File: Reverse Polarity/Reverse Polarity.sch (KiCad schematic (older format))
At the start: 16 parts, among them P1 CONN_01X04, P2 CONN_01X04, P3 CONN_01X04, P4 CONN_01X04, P5 CONN_01X04, P6 CONN_01X04, P7 CONN_01X04, P8 CONN_01X04

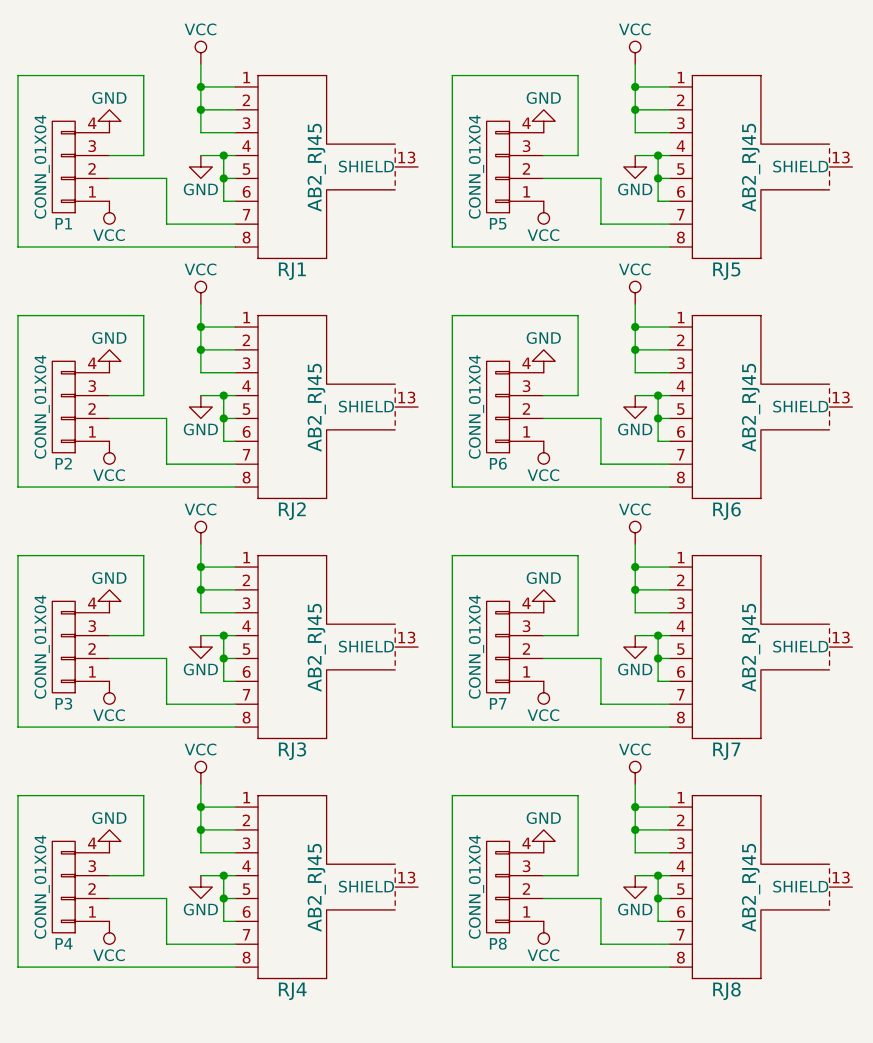
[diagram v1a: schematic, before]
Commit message: I had the ethernet plugs flopped, whoops
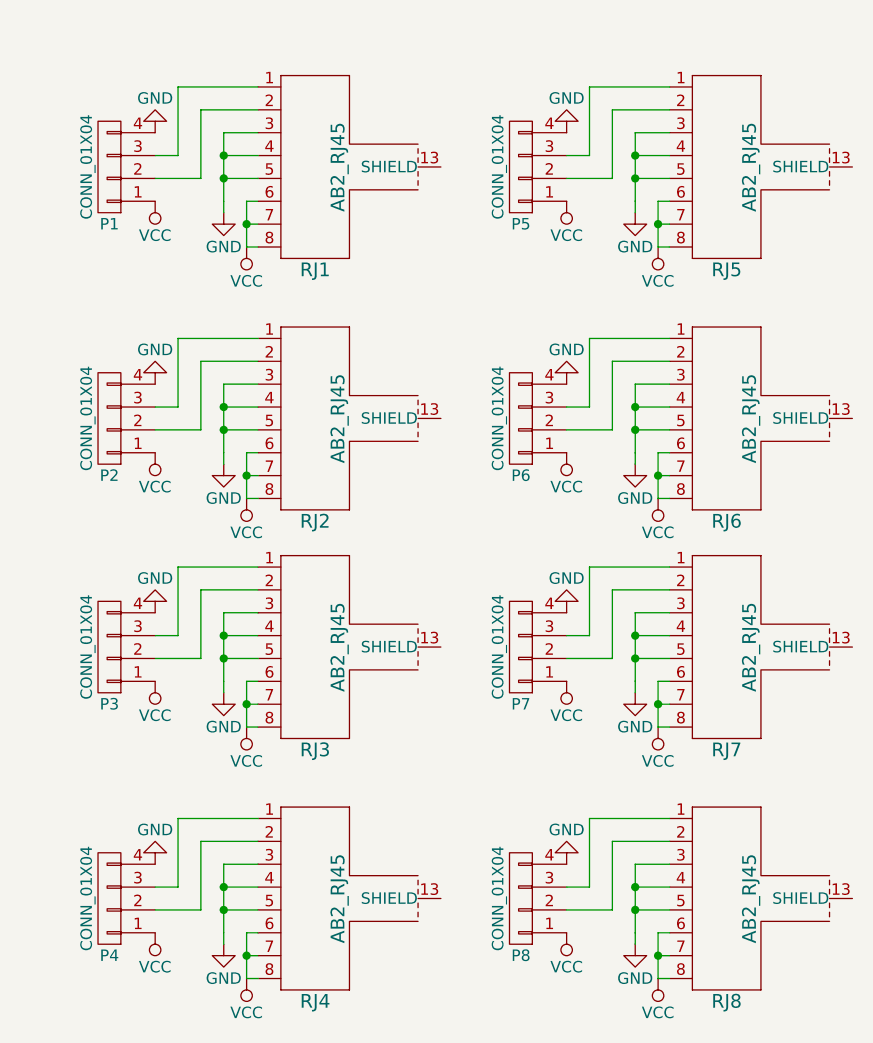
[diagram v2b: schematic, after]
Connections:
- net GND: now also RJ1.3, RJ2.3, RJ3.3, RJ4.3, RJ5.3, RJ6.3, RJ7.3, RJ8.3; no longer RJ1.6, RJ2.6, RJ3.6, RJ4.6, RJ5.6, RJ6.6, RJ7.6, RJ8.6
- net VCC: now also RJ1.6, RJ1.7, RJ1.8, RJ2.6, RJ2.7, RJ2.8, RJ3.6, RJ3.7, RJ3.8, RJ4.6, RJ4.7, RJ4.8, RJ5.6, RJ5.7, RJ5.8, RJ6.6, RJ6.7, RJ6.8, RJ7.6, RJ7.7, RJ7.8, RJ8.6, RJ8.7, RJ8.8; no longer RJ1.1, RJ1.2, RJ1.3, RJ2.1, RJ2.2, RJ2.3, RJ3.1, RJ3.2, RJ3.3, RJ4.1, RJ4.2, RJ4.3, RJ5.1, RJ5.2, RJ5.3, RJ6.1, RJ6.2, RJ6.3, RJ7.1, RJ7.2, RJ7.3, RJ8.1, RJ8.2, RJ8.3
- net at P1.2 (P2): now also RJ1.2; no longer RJ1.7
- net at P1.3 (P3): now also RJ1.1; no longer RJ1.8
- net at P2.2 (P2): now also RJ2.2; no longer RJ2.7
- net at P2.3 (P3): now also RJ2.1; no longer RJ2.8
- net at P3.2 (P2): now also RJ3.2; no longer RJ3.7
- net at P3.3 (P3): now also RJ3.1; no longer RJ3.8
- net at P4.2 (P2): now also RJ4.2; no longer RJ4.7
- net at P4.3 (P3): now also RJ4.1; no longer RJ4.8
- net at P5.2 (P2): now also RJ5.2; no longer RJ5.7
- net at P5.3 (P3): now also RJ5.1; no longer RJ5.8
- net at P6.2 (P2): now also RJ6.2; no longer RJ6.7
- net at P6.3 (P3): now also RJ6.1; no longer RJ6.8
- net at P7.2 (P2): now also RJ7.2; no longer RJ7.7
- net at P7.3 (P3): now also RJ7.1; no longer RJ7.8
- net at P8.2 (P2): now also RJ8.2; no longer RJ8.7
- net at P8.3 (P3): now also RJ8.1; no longer RJ8.8
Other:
- moved on the sheet: P1, RJ1

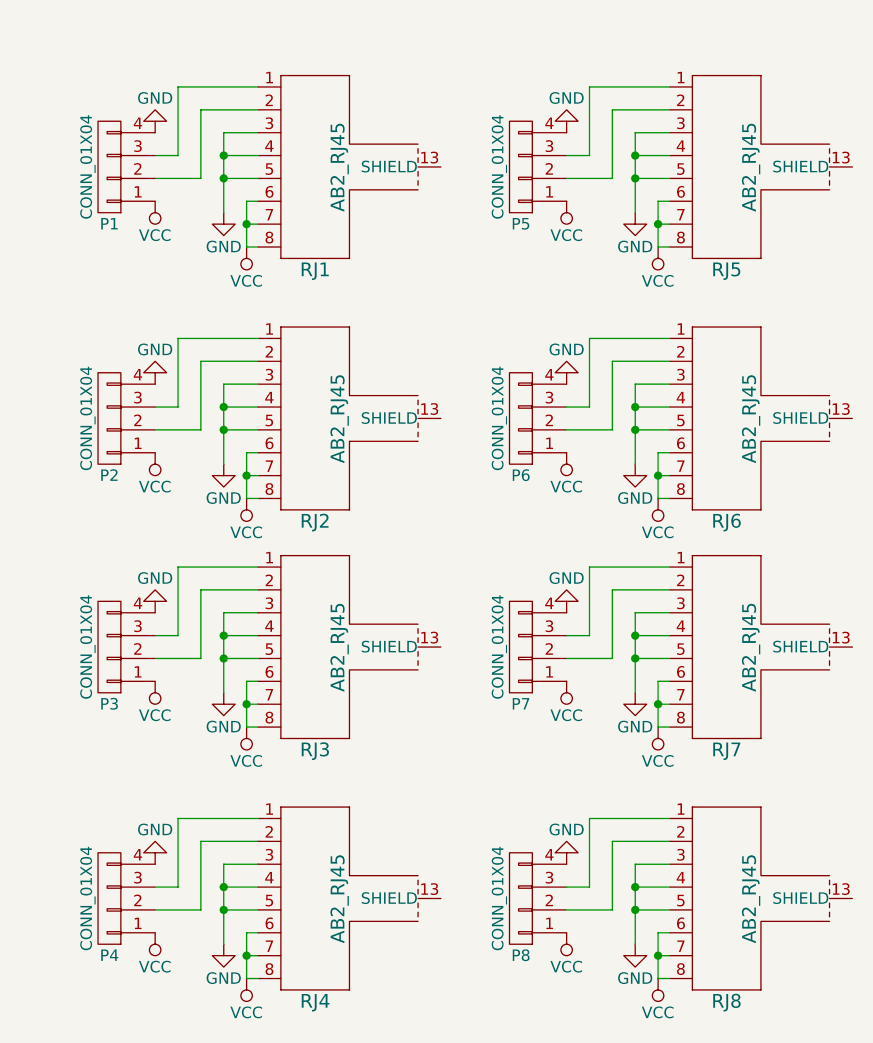
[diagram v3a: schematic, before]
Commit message: * Remove dead extender * Add normal polarity (which was what I was calling reverse polarity) * Fix reverse polarity to actually be reversed
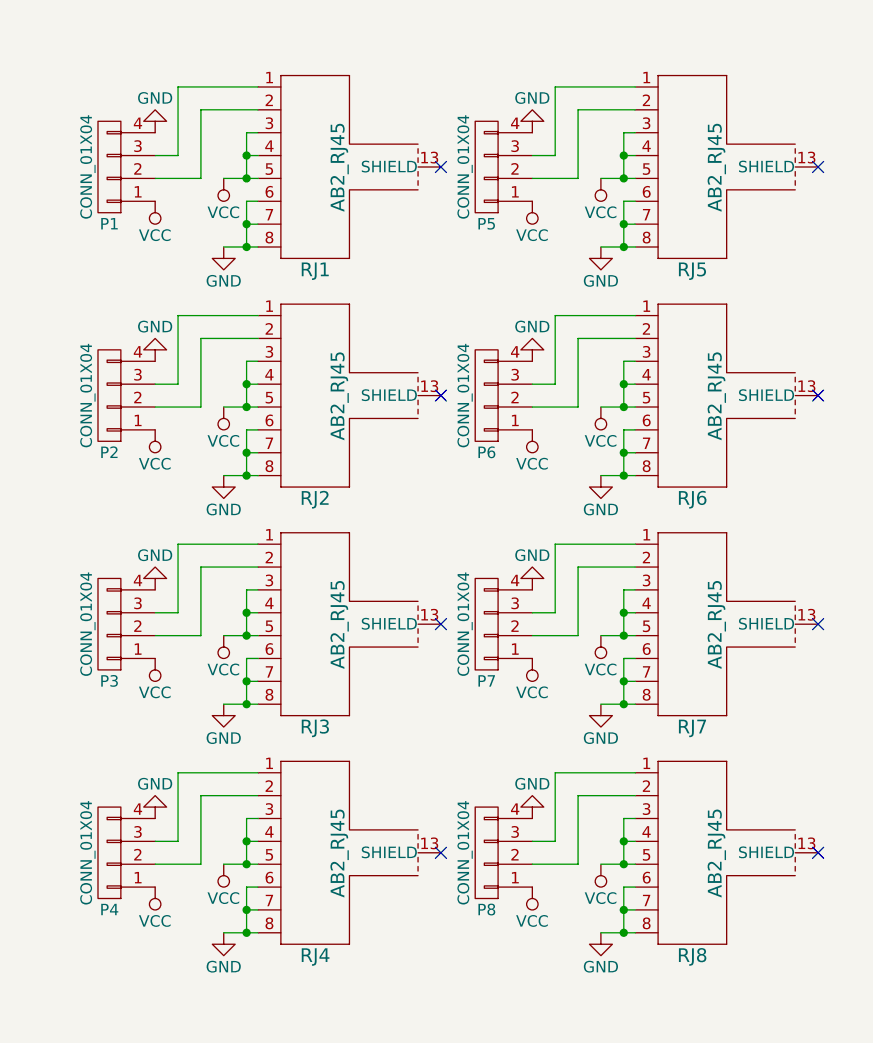
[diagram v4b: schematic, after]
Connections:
- net GND: now also RJ1.6, RJ1.7, RJ1.8, RJ2.6, RJ2.7, RJ2.8, RJ3.6, RJ3.7, RJ3.8, RJ4.6, RJ4.7, RJ4.8, RJ5.6, RJ5.7, RJ5.8, RJ6.6, RJ6.7, RJ6.8, RJ7.6, RJ7.7, RJ7.8, RJ8.6, RJ8.7, RJ8.8; no longer RJ1.3, RJ1.4, RJ1.5, RJ2.3, RJ2.4, RJ2.5, RJ3.3, RJ3.4, RJ3.5, RJ4.3, RJ4.4, RJ4.5, RJ5.3, RJ5.4, RJ5.5, RJ6.3, RJ6.4, RJ6.5, RJ7.3, RJ7.4, RJ7.5, RJ8.3, RJ8.4, RJ8.5
- net VCC: now also RJ1.3, RJ1.4, RJ1.5, RJ2.3, RJ2.4, RJ2.5, RJ3.3, RJ3.4, RJ3.5, RJ4.3, RJ4.4, RJ4.5, RJ5.3, RJ5.4, RJ5.5, RJ6.3, RJ6.4, RJ6.5, RJ7.3, RJ7.4, RJ7.5, RJ8.3, RJ8.4, RJ8.5; no longer RJ1.6, RJ1.7, RJ1.8, RJ2.6, RJ2.7, RJ2.8, RJ3.6, RJ3.7, RJ3.8, RJ4.6, RJ4.7, RJ4.8, RJ5.6, RJ5.7, RJ5.8, RJ6.6, RJ6.7, RJ6.8, RJ7.6, RJ7.7, RJ7.8, RJ8.6, RJ8.7, RJ8.8
- no-connect marks 0 -> 8
